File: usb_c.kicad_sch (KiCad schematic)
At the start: 23 parts, among them J1 USB_C_Receptacle, U1 MIC5363-3.3YMT, U2 HD3SS3220, U3 MG2040

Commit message: SDReWire: Footprint assigment
Signed-off-by: Dominik Sliwa <dominik@sliwa.io>
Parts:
- C2: footprint Capacitor_SMD:C_0603_1608Metric -> Capacitor_SMD:C_0402_1005Metric
- FB2: footprint Resistor_SMD:R_0402_1005Metric -> Resistor_SMD:R_0603_1608Metric
- J1: footprint Connector_USB:USB_C_Receptacle_Amphenol_12401610E4-2A -> Custom:USB_C_Receptacle_Molex_1054500101
- RN1: footprint (none) -> Resistor_SMD:R_0402_1005Metric
- gave numbers to parts that had none: 1
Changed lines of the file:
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@@
   (symbol (lib_id "power:GND") (at 94.615 99.06 270) (unit 1)
     (in_bom yes) (on_board yes)
-    (property "Reference" "#PWR?" (id 0) (at 88.265 99.06 0)
+    (property "Reference" "#PWR024" (id 0) (at 88.265 99.06 0)
       (effects (font (size 1.27 1.27)) hide)
     )
@@
   (symbol (lib_id "power:GND") (at 124.46 99.06 90) (unit 1)
     (in_bom yes) (on_board yes)
-    (property "Reference" "#PWR?" (id 0) (at 130.81 99.06 0)
+    (property "Reference" "#PWR025" (id 0) (at 130.81 99.06 0)
       (effects (font (size 1.27 1.27)) hide)
     )
@@
     (property "Reference" "C2" (id 0) (at 106.045 41.275 0))
     (property "Value" "10uF" (id 1) (at 106.68 45.72 0))
-    (property "Footprint" "Capacitor_SMD:C_0603_1608Metric" (id 2) (at 103.505 43.18 0)
+    (property "Footprint" "Capacitor_SMD:C_0402_1005Metric" (id 2) (at 103.505 43.18 0)
       (effects (font (size 1.27 1.27)) hide)
     )
@@
   (symbol (lib_id "Device:C_Small") (at 118.745 99.06 270) (unit 1)
     (in_bom yes) (on_board yes)
-    (property "Reference" "C?" (id 0) (at 116.84 97.155 90))
+    (property "Reference" "C21" (id 0) (at 116.84 97.155 90))
     (property "Value" "0.1uF" (id 1) (at 122.555 97.155 90))
     (property "Footprint" "Capacitor_SMD:C_0402_1005Metric" (id 2) (at 118.745 99.06 0)
@@
     (property "Reference" "FB2" (id 0) (at 59.055 76.835 90))
     (property "Value" "1k@100MHz" (id 1) (at 59.055 79.375 90))
-    (property "Footprint" "Resistor_SMD:R_0402_1005Metric" (id 2) (at 59.055 84.963 90)
+    (property "Footprint" "Resistor_SMD:R_0603_1608Metric" (id 2) (at 59.055 84.963 90)
       (effects (font (size 1.27 1.27)) hide)
     )
@@
       (effects (font (size 1.27 1.27)) (justify left))
     )
-    (property "Footprint" "" (id 2) (at 201.168 36.195 90)
+    (property "Footprint" "Resistor_SMD:R_0402_1005Metric" (id 2) (at 201.168 36.195 90)
       (effects (font (size 1.27 1.27)) hide)
     )
@@
     (property "Reference" "J1" (id 0) (at 37.465 75.565 0))
     (property "Value" "USB_C_Receptacle" (id 1) (at 37.465 78.105 0))
-    (property "Footprint" "Connector_USB:USB_C_Receptacle_Amphenol_12401610E4-2A" (id 2) (at 37.465 108.585 0)
-      (effects (font (size 1.27 1.27)) hide)
-    )
+    (property "Footprint" "Custom:USB_C_Receptacle_Molex_1054500101" (id 2) (at 37.465 108.585 0)
+      (effects (font (size 1.27 1.27)) hide)
+    )

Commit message: SDReWire: rename FTDI_GPIO to SD_MUX_SEL and fix assigment
Resistor array had a wrong footprint

Signed-off-by: Dominik Sliwa <dominik@sliwa.io>
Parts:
- RN1: footprint Resistor_SMD:R_0402_1005Metric -> Resistor_SMD:R_Array_Convex_4x0402
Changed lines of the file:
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@@
       (effects (font (size 1.27 1.27)) (justify left))
     )
-    (property "Footprint" "Resistor_SMD:R_0402_1005Metric" (id 2) (at 201.168 36.195 90)
+    (property "Footprint" "Resistor_SMD:R_Array_Convex_4x0402" (id 2) (at 201.168 36.195 90)
       (effects (font (size 1.27 1.27)) hide)
     )

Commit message: SDReWire: fix assigments
modify few components footprint assigments

Signed-off-by: Dominik Sliwa <dominik@sliwa.io>
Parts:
- U3: footprint Glasgow:UDFN-18-3EP_5.5x1.5mm_P0.5mm_EP0.5x0.5mm -> Custom:UDFN-18-3EP_5.5x1.5mm_P0.5mm_EP0.5x0.5mm
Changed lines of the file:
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@@
   (junction (at 148.59 47.625) (diameter 1.016) (color 0 0 0 0))
   (junction (at 152.4 38.735) (diameter 1.016) (color 0 0 0 0))
-  (no_connect (at 135.255 154.305))
   (no_connect (at 135.255 144.145))
   (no_connect (at 135.255 126.365))
+  (no_connect (at 135.255 154.305))
+  (no_connect (at 48.895 139.065))
+  (no_connect (at 48.895 141.605))
   (no_connect (at 135.255 128.905))
+  (no_connect (at 135.255 141.605))
+  (no_connect (at 135.255 146.685))
   (no_connect (at 135.255 151.765))
-  (no_connect (at 135.255 141.605))
-  (no_connect (at 48.895 141.605))
-  (no_connect (at 48.895 139.065))
-  (no_connect (at 135.255 146.685))
   (wire (pts (xy 26.035 151.13) (xy 26.035 149.225))
     (stroke (width 0) (type solid) (color 0 0 0 0))
@@
     (property "Reference" "U3" (id 0) (at 50.8 22.86 90))
     (property "Value" "MG2040" (id 1) (at 50.8 25.4 90))
-    (property "Footprint" "Glasgow:UDFN-18-3EP_5.5x1.5mm_P0.5mm_EP0.5x0.5mm" (id 2) (at 61.341 44.831 0)
-      (effects (font (size 1.27 1.27)) hide)
-    )
+    (property "Footprint" "Custom:UDFN-18-3EP_5.5x1.5mm_P0.5mm_EP0.5x0.5mm" (id 2) (at 61.341 44.831 0)
+      (effects (font (size 1.27 1.27)) hide)
+    )

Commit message: SDReWire: fix MIC5363 symbol
Signed-off-by: Dominik Sliwa <dominik@sliwa.io>
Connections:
- net +5V: now also U1.4 (VIN), U1.6 (EN); no longer U1.1 (VIN), U1.3 (EN)
- net GND: now also U1.3 (GND), U1.7 (ePad); no longer U1.2 (GND)

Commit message: usb_c.kicad_sch: swap usb 3 pairs at MG2040
Signed-off-by: Dominik Sliwa <dominik@sliwa.io>
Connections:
- net CTX1+: now also U3.4; no longer U3.5
- net CTX1-: now also U3.5; no longer U3.4
- net CTX2+: now also U3.10; no longer U3.11
- net CTX2-: now also U3.11; no longer U3.10
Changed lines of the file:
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@@
     (effects (font (size 1.27 1.27)) (justify left bottom))
   )
-  (label "CTX1-" (at 36.83 38.735 0)
+  (label "CTX1+" (at 36.83 38.735 0)
     (effects (font (size 1.27 1.27)) (justify left bottom))
   )
-  (label "CTX1+" (at 36.83 41.275 0)
+  (label "CTX1-" (at 36.83 41.275 0)
     (effects (font (size 1.27 1.27)) (justify left bottom))
   )
@@
     (effects (font (size 1.27 1.27)) (justify left bottom))
   )
-  (label "CTX2-" (at 36.83 53.975 0)
+  (label "CTX2+" (at 36.83 53.975 0)
     (effects (font (size 1.27 1.27)) (justify left bottom))
   )
-  (label "CTX2+" (at 36.83 56.515 0)
+  (label "CTX2-" (at 36.83 56.515 0)
     (effects (font (size 1.27 1.27)) (justify left bottom))
   )

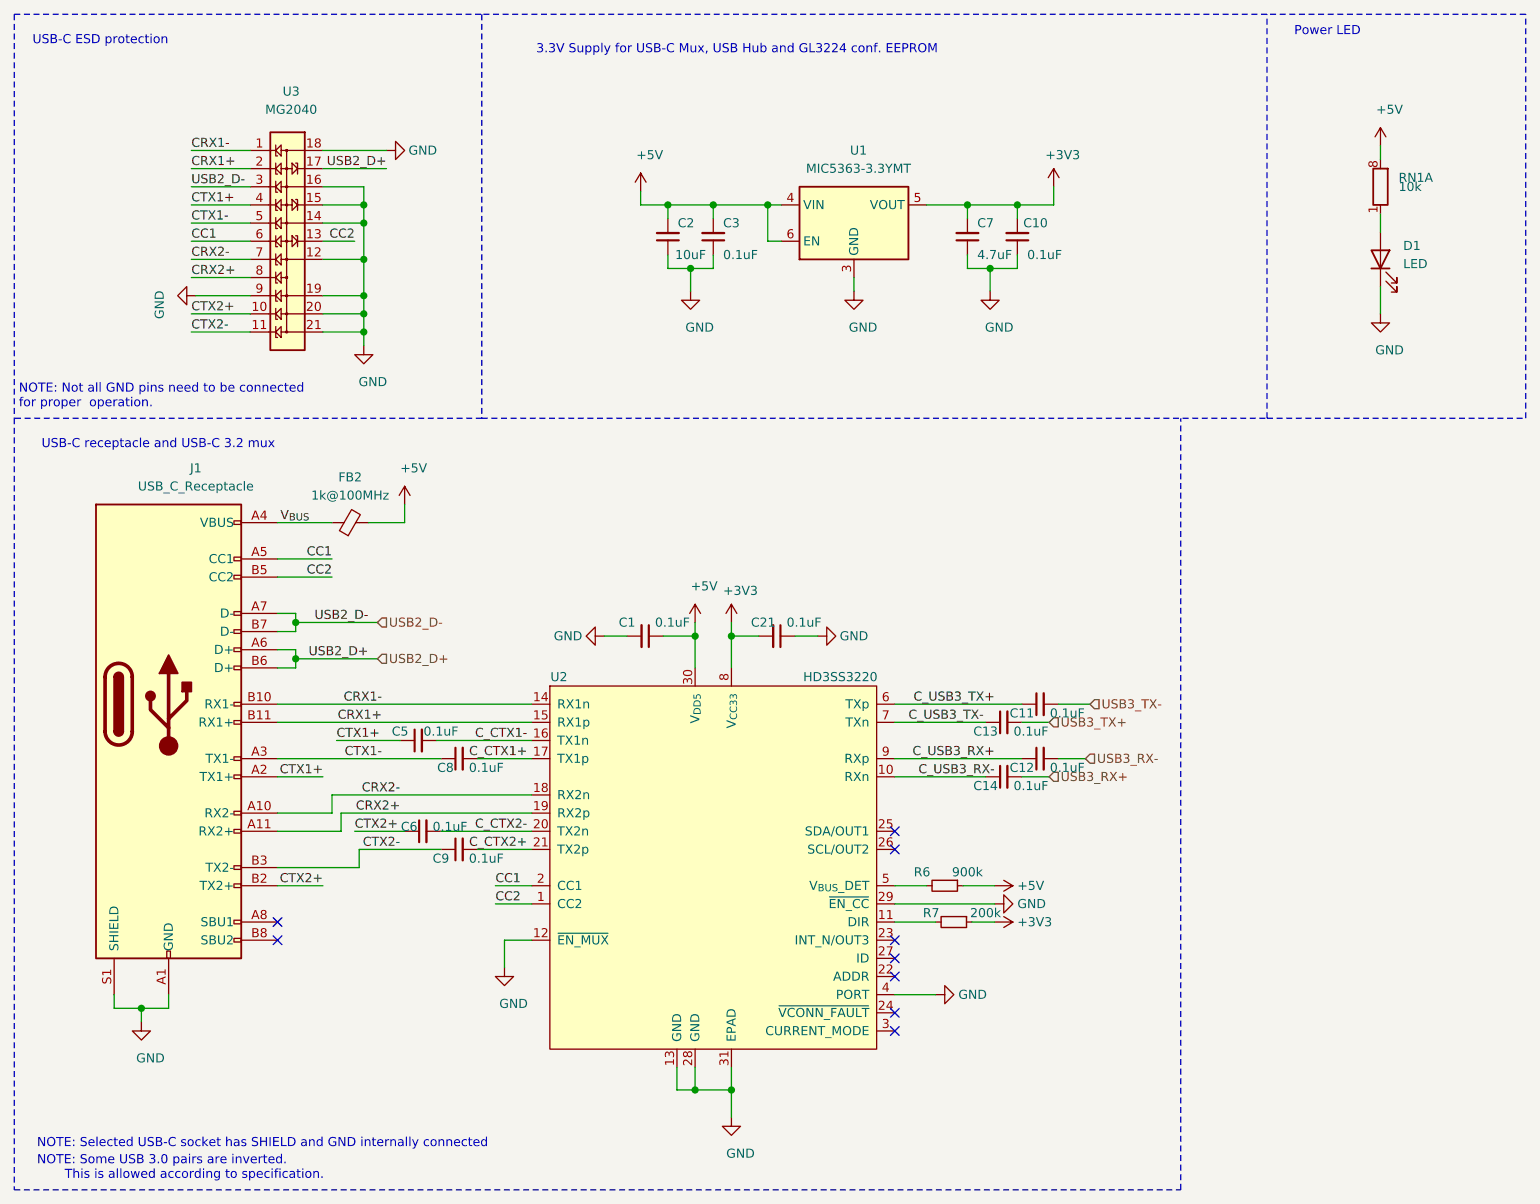
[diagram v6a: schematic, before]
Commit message: sdrewire: pcb v1
Some itra-pair inversions for easier routing.
Fixed crystal pinouts
sd power p-fet changed for smaller package

Signed-off-by: Dominik Sliwa <dominik@sliwa.io>
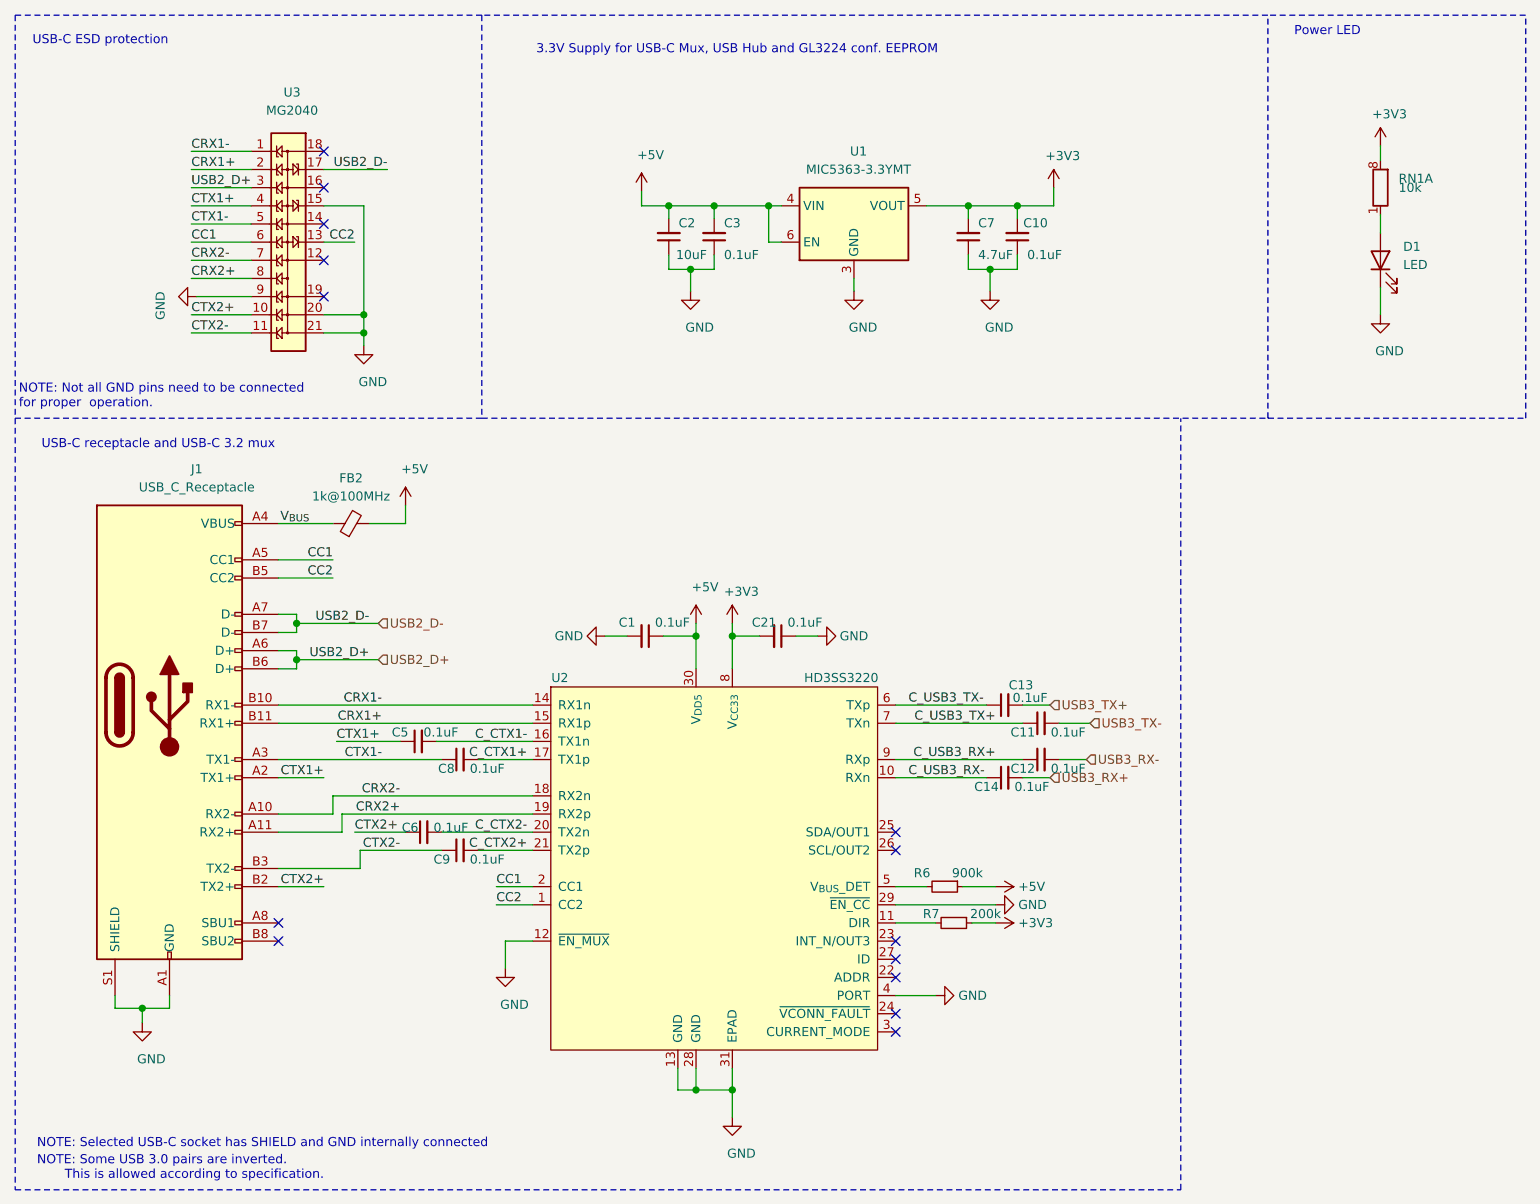
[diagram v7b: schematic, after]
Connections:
- net +3V3: now also RN1.8 (R1.2)
- net +5V: no longer RN1.8 (R1.2)
- net C_USB3_RX-: now also C14.1, U2.10 (RXn)
- net C_USB3_TX+: now also U2.7 (TXn); no longer U2.6 (TXp)
- net C_USB3_TX-: now also U2.6 (TXp); no longer U2.7 (TXn)
- net GND: no longer U3.12, U3.14, U3.16, U3.18, U3.19
- net USB2_D+: now also U3.3; no longer U3.17
- net USB2_D-: now also U3.17; no longer U3.3
- no-connect marks 9 -> 14
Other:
- moved on the sheet: C11, C13
